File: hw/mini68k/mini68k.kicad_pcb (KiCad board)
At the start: 2 copper layers, 147.3 x 100.3 mm, 29 parts, among them J1 Jack-DC, J2 6-bit input port, J3 8-bit output port, J4 FTDI header, SW1 SW_SPDT, SW2 SW_Push, U1 HM62256BLP-7, U2 68008D, U3 L7805, U4 28C256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

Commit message: better fills
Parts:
- added J5: FTDI header COM2, Connector_PinHeader_2.54mm:PinHeader_1x06_P2.54mm_Vertical, F.Cu at (229.9, 83.8)
- added JP2: Jumper, Connector_PinHeader_2.54mm:PinHeader_1x02_P2.54mm_Vertical, F.Cu at (224.8, 71.1)
- J4: value FTDI header -> FTDI header COM1
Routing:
- net GND: track 697.5 -> 155.5 mm, vias 9 -> 12
- net VCC: track 493.9 -> 35.6 mm, vias 2 -> 3
- net TX2: track 0.00 -> 82.3 mm, vias 0 -> 1
- net RX2: track 0.00 -> 77.5 mm, vias 0 -> 1
- net A9: track 155.8 -> 131.3 mm
- net OP7: track 46.5 -> 26.5 mm
- net A4: track 146.8 -> 132.5 mm
- net A5: track 92.5 -> 81.0 mm
- net A15: track 144.1 -> 133.4 mm
- net A7: track 100.5 -> 90.1 mm
- net Net-(J5-Pad3): track 0.00 -> 10.4 mm
- net A3: track 157.4 -> 149.8 mm
- net A16: track 125.3 -> 117.8 mm
- net CLK: track 207.3 -> 199.9 mm, vias 1 -> 2
- net A6: track 89.4 -> 84.2 mm
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
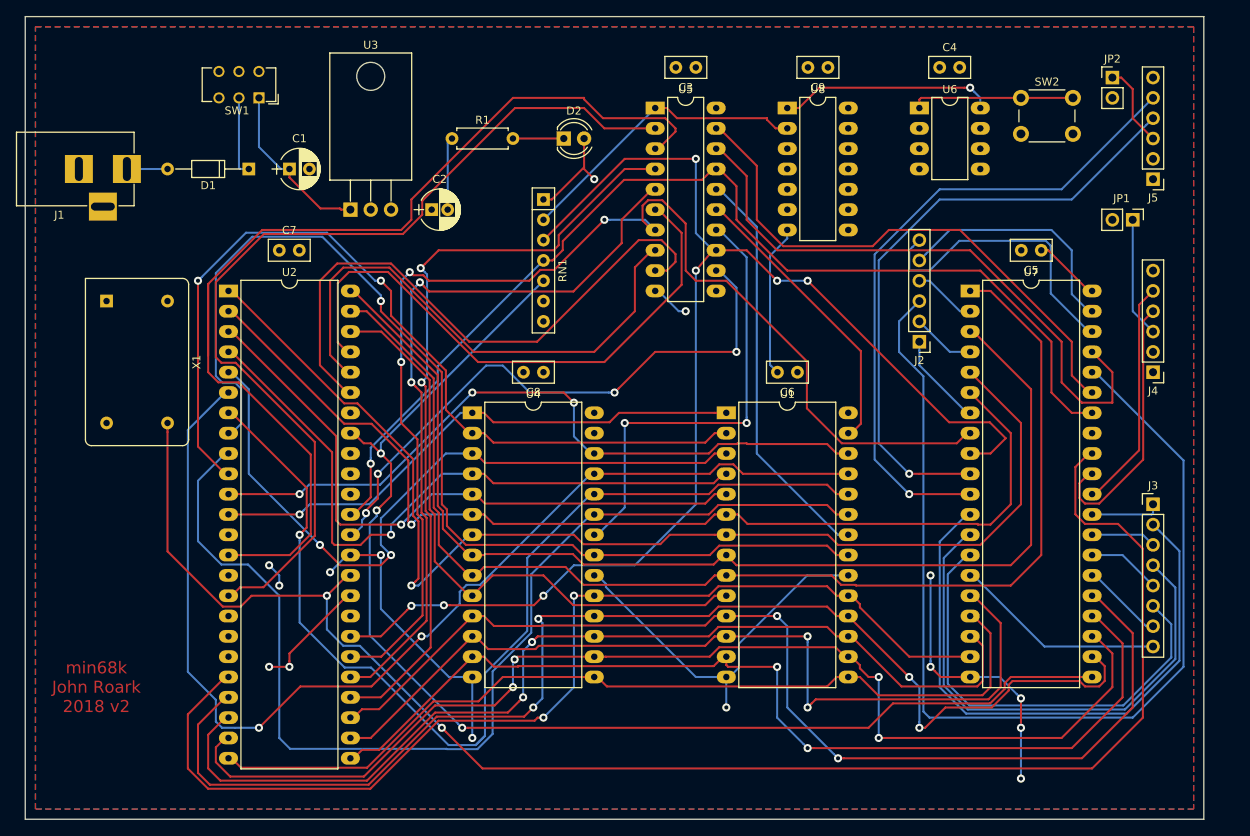
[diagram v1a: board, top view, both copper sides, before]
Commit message: more updated footprints and 3d
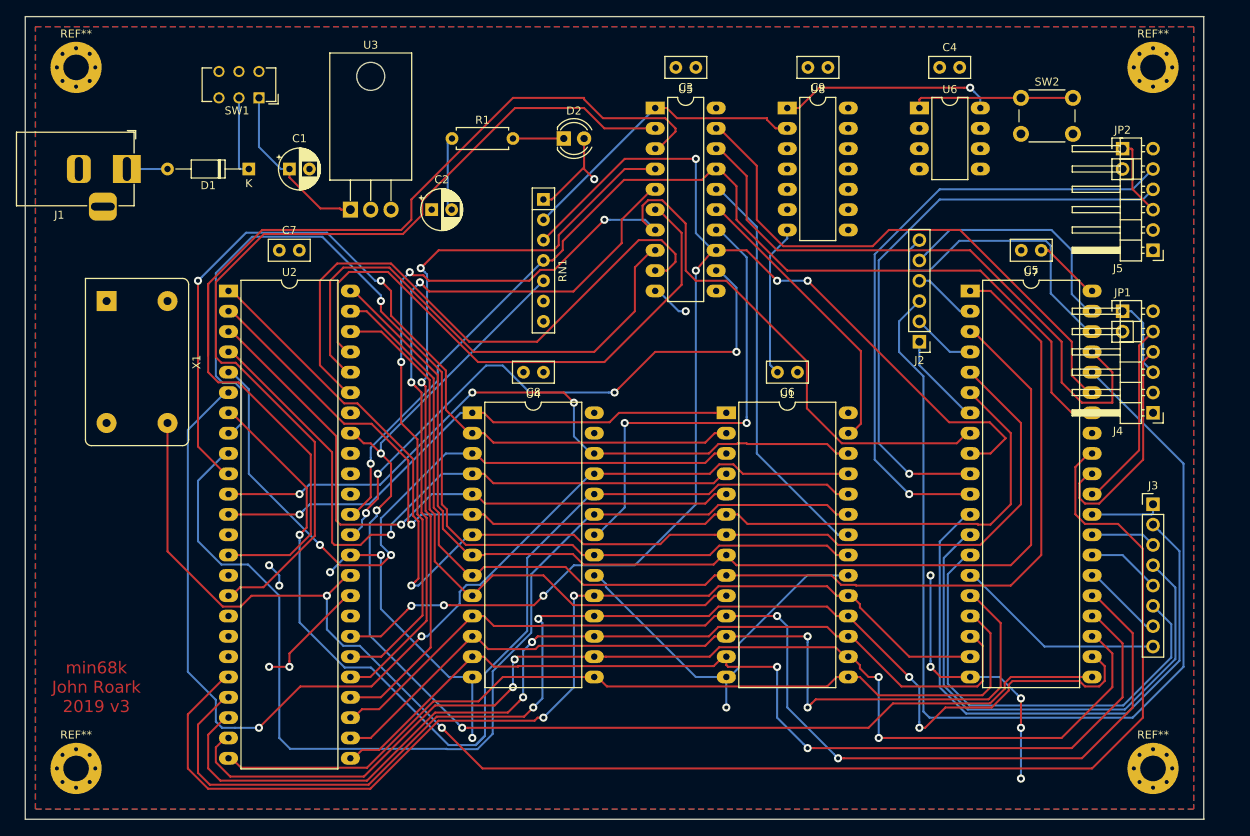
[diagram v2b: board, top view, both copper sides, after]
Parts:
- added REF**: MountingHole_3.2mm_M3_Pad_Via, MountingHole:MountingHole_3.2mm_M3_Pad_Via, F.Cu at (95.2, 157.5)
- added REF**: MountingHole_3.2mm_M3_Pad_Via, MountingHole:MountingHole_3.2mm_M3_Pad_Via, F.Cu at (95.2, 69.8)
- added REF**: MountingHole_3.2mm_M3_Pad_Via, MountingHole:MountingHole_3.2mm_M3_Pad_Via, F.Cu at (229.9, 157.5)
- added REF**: MountingHole_3.2mm_M3_Pad_Via, MountingHole:MountingHole_3.2mm_M3_Pad_Via, F.Cu at (229.9, 69.8)
- C1: footprint Capacitors_THT:CP_Radial_D5.0mm_P2.50mm -> Capacitor_THT:CP_Radial_D5.0mm_P2.50mm
- C2: footprint Capacitors_THT:CP_Radial_D5.0mm_P2.00mm -> Capacitor_THT:CP_Radial_D5.0mm_P2.50mm
- D1: footprint Diodes_THT:D_DO-35_SOD27_P10.16mm_Horizontal -> Diode_THT:D_DO-35_SOD27_P10.16mm_Horizontal
- D2: footprint LEDs:LED_D4.0mm -> LED_THT:LED_D4.0mm
- J1: footprint Connectors:BARREL_JACK -> Connector_BarrelJack:BarrelJack_Horizontal
- J4, J5: footprint Connector_PinHeader_2.54mm:PinHeader_1x06_P2.54mm_Vertical -> Connector_PinHeader_2.54mm:PinHeader_1x06_P2.54mm_Horizontal
- JP1: footprint Pin_Headers:Pin_Header_Straight_1x02_Pitch2.54mm -> Connector_PinHeader_2.54mm:PinHeader_1x02_P2.54mm_Vertical
- R1: footprint Resistors_THT:R_Axial_DIN0207_L6.3mm_D2.5mm_P7.62mm_Horizontal -> Resistor_THT:R_Axial_DIN0207_L6.3mm_D2.5mm_P7.62mm_Horizontal
- RN1: footprint Resistors_THT:R_Array_SIP7 -> Resistor_THT:R_Array_SIP7
- SW2: footprint Buttons_Switches_THT:SW_PUSH_6mm -> Button_Switch_THT:SW_PUSH_6mm
- U3: footprint TO_SOT_Packages_THT:TO-220-3_Horizontal -> Package_TO_SOT_THT:TO-220-3_Horizontal_TabDown
- X1: footprint Oscillators:Oscillator_DIP-14 -> Oscillator:Oscillator_DIP-14_LargePads
- moved JP1 11.5 mm to (226.1, 100.3), turned to 0 degrees
- moved JP2 8.98 mm to (226.1, 80.0)
- moved J5 8.89 mm to (229.9, 92.7)
- moved J4 5.08 mm to (229.9, 113.0)
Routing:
- net Net-(J4-Pad3): track 15.0 -> 9.84 mm
- net TX1: track 28.8 -> 23.7 mm
- net RX1: track 33.5 -> 28.4 mm
- net TX2: track 82.3 -> 78.6 mm
- net RX2: track 77.5 -> 73.8 mm
- net Net-(J5-Pad3): track 10.4 -> 9.84 mm
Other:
- board text added: "min68k John Roark 2019 v3"
- board text removed: "min68k John Roark 2018 v2"

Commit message: better 3d
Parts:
- J4, J5: footprint Connector_PinHeader_2.54mm:PinHeader_1x06_P2.54mm_Horizontal -> Connector_PinHeader_2.54mm:PinHeader_1x06_P2.54mm_Vertical
- SW1: footprint Buttons_Switches_THT:SW_CuK_JS202011CQN_DPDT_Straight -> Button_Switch_THT:SW_E-Switch_EG1271_DPDT

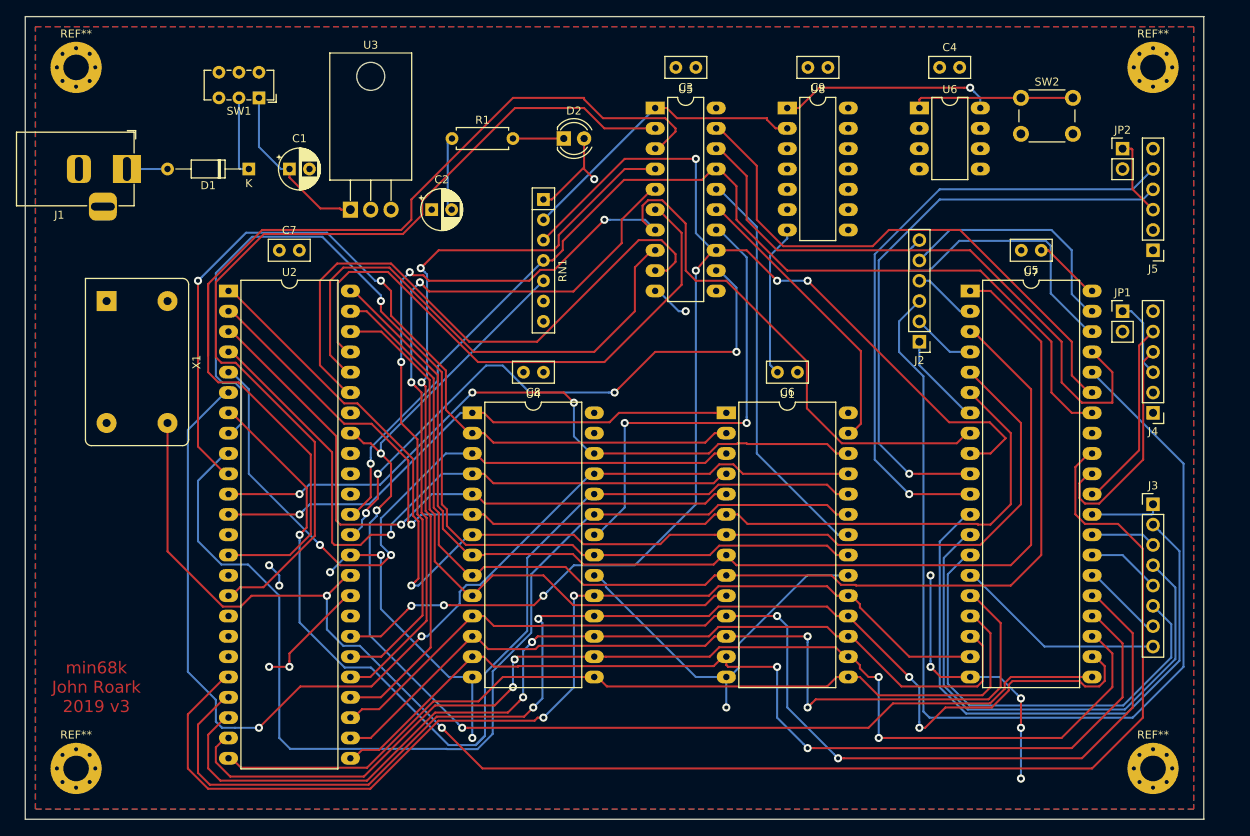
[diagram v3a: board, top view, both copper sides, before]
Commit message: jumpers for 27256/28256
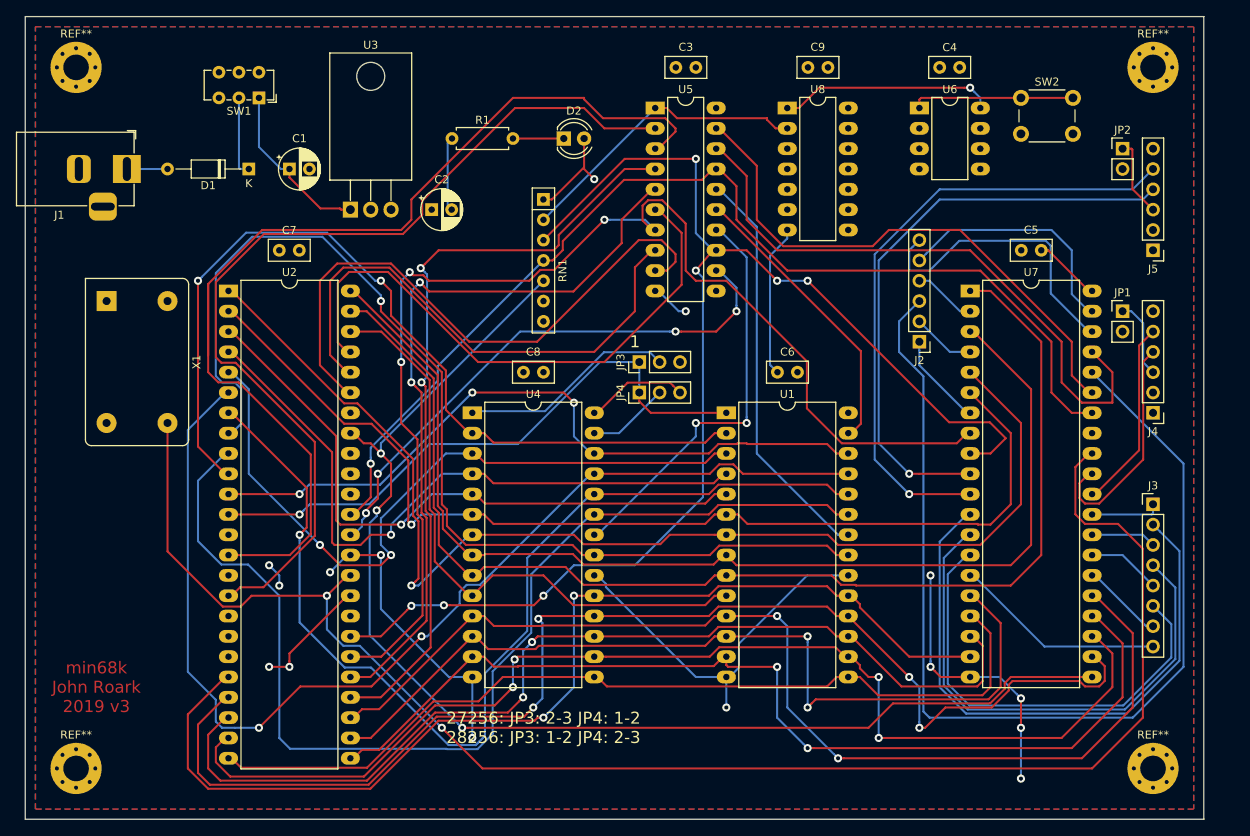
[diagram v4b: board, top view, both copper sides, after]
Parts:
- added JP3: Jumper_3_Open, Connector_PinHeader_2.54mm:PinHeader_1x03_P2.54mm_Vertical, F.Cu at (165.7, 106.7)
- added JP4: Jumper_3_Open, Connector_PinHeader_2.54mm:PinHeader_1x03_P2.54mm_Vertical, F.Cu at (165.7, 110.5)
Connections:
- U4 pad 1: A14 -> ROM_PIN1
- U4 pad 27: VCC -> ROM_PIN27
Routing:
- net ROM_PIN1: track 0.00 -> 26.7 mm
- net VCC: track 35.6 -> 48.4 mm
- net ROM_PIN27: track 0.00 -> 10.3 mm
- net A14: track 68.5 -> 75.6 mm
- net HALT: track 74.7 -> 68.9 mm
- net ROM_OE: track 57.0 -> 51.8 mm
- net DTACK: track 170.1 -> 170.8 mm
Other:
- board text added: "1"
- board text added: "27256: JP3: 2-3 JP4: 1-2 28256: JP3: 1-2 JP4: 2-3"

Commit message: labels
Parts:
- renumbered SW1 to ON, SW2 to RESET
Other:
- board text added: "GND"
- board text added: "RX"
- board text added: "TX"
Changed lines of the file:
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@@
   (general
     (thickness 1.6)
-    (drawings 7)
+    (drawings 15)
     (tracks 1110)
     (zones 0)
@@
     (descr https://www.omron.com/ecb/products/pdf/en-b3f.pdf)
     (tags "tact sw push 6mm")
-    (fp_text reference SW2 (at 3.25 -2) (layer F.SilkS)
+    (fp_text reference RESET (at 3.25 -2) (layer F.SilkS)
       (effects (font (size 1 1) (thickness 0.15)))
     )
@@
     (descr "E-Switch sub miniature slide switch, EG series, DPDT, http://spec_sheets.e-switch.com/specs/P040047.pdf")
     (tags "switch DPDT")
-    (fp_text reference SW1 (at 2.5 -1.65 180) (layer F.SilkS)
+    (fp_text reference ON (at 0 -2.54 180) (layer F.SilkS)
       (effects (font (size 1 1) (thickness 0.15)))
     )
@@
     )
   )
+  (gr_text GND (at 234.5 92.71) (layer F.SilkS)
+    (effects (font (size 1 1) (thickness 0.25)) (justify right))
+  )
+  (gr_text RX (at 232.41 85.09) (layer F.SilkS)
+    (effects (font (size 1 1) (thickness 0.25)))
+  )
+  (gr_text TX (at 232.41 82.55) (layer F.SilkS)
+    (effects (font (size 1 1) (thickness 0.25)))
+  )
+  (gr_text GND (at 234.5 113.03) (layer F.SilkS)
+    (effects (font (size 1 1) (thickness 0.25)) (justify right))
+  )
+  (gr_text RX (at 232.41 105.41) (layer F.SilkS)
+    (effects (font (size 1 1) (thickness 0.25)))
+  )
+  (gr_text TX (at 232.41 102.87) (layer F.SilkS)
+    (effects (font (size 1 1) (thickness 0.25)))
+  )
+  (gr_text 1 (at 232.41 124.46) (layer F.SilkS)
+    (effects (font (size 1.5 1.5) (thickness 0.3)))
+  )
+  (gr_text 1 (at 198.12 104.14) (layer F.SilkS)
+    (effects (font (size 1.5 1.5) (thickness 0.3)))
+  )
   (gr_text "27256: JP3: 2-3 JP4: 1-2\n28256: JP3: 1-2 JP4: 2-3" (at 153.67 152.4) (layer F.SilkS)

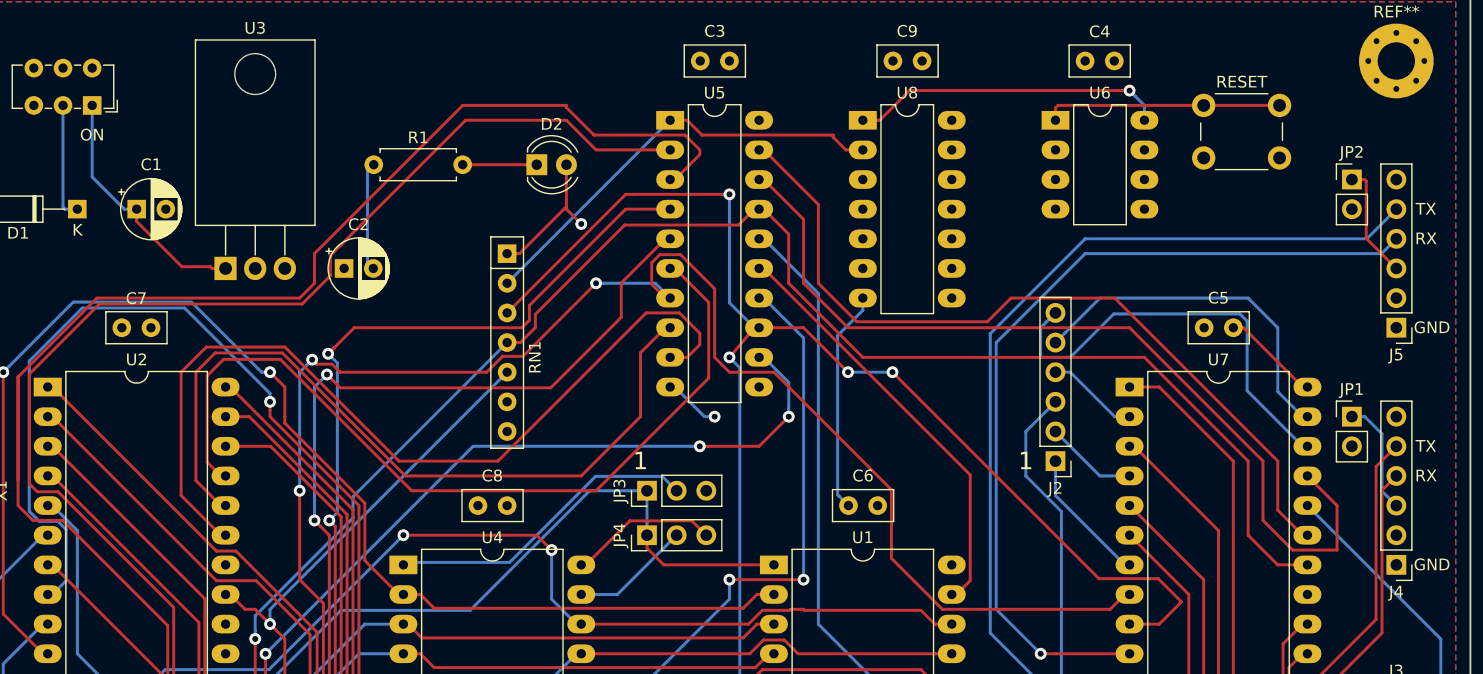
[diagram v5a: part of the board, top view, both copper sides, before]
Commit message: correct ram pinout... update symbols
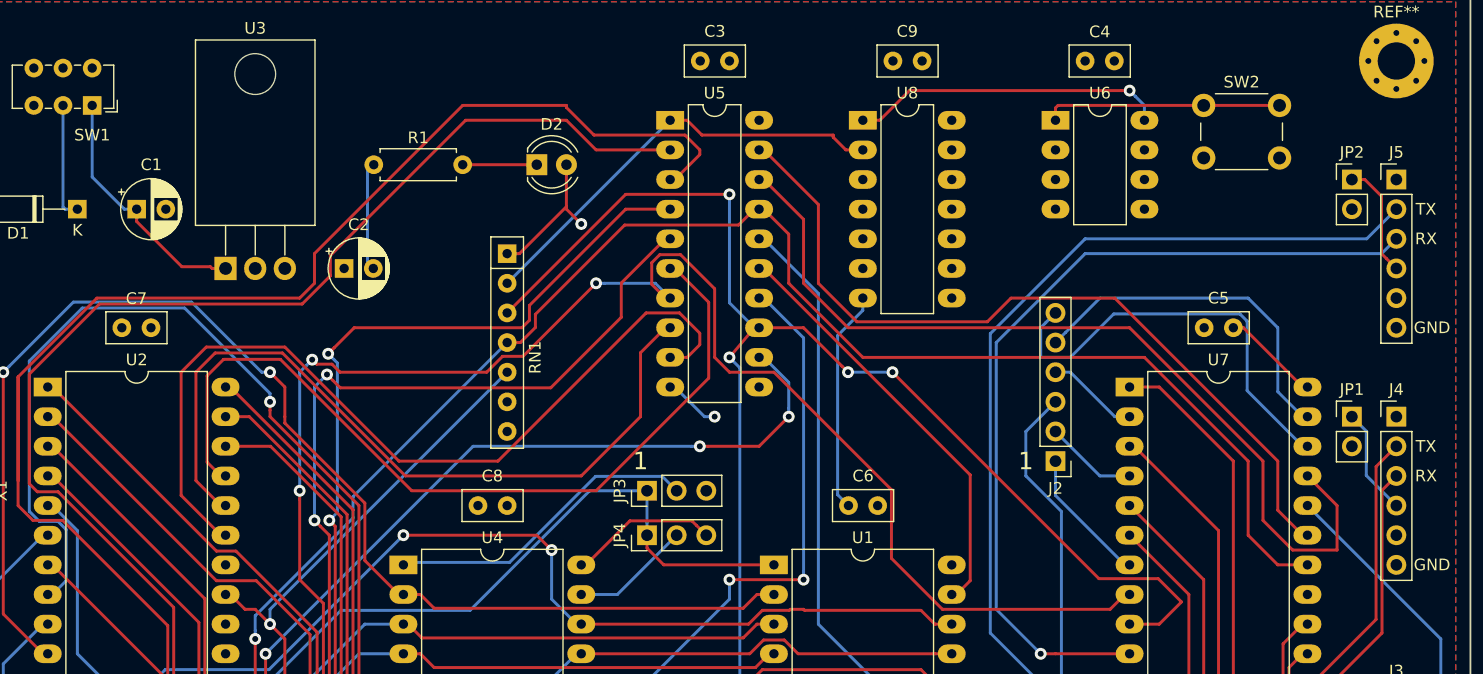
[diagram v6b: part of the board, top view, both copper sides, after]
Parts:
- U4: value 28C256 -> 28C256/27C256
- moved J4 12.7 mm to (229.9, 100.3), turned to 0 degrees
- moved J5 12.7 mm to (229.9, 80.0), turned to 0 degrees
- renumbered ON to SW1, RESET to SW2
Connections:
- J4 pad 1: GND -> Net-(J4-Pad1)
- J4 pad 2: Net-(J4-Pad2) -> TX1
- J4 pad 3: Net-(J4-Pad3) -> RX1
- J4 pad 4: RX1 -> Net-(J4-Pad4)
- J4 pad 5: TX1 -> Net-(J4-Pad5)
- J4 pad 6: Net-(J4-Pad6) -> GND
- J5 pad 1: GND -> Net-(J5-Pad1)
- J5 pad 2: Net-(J5-Pad2) -> TX2
- J5 pad 3: Net-(J5-Pad3) -> RX2
- J5 pad 4: RX2 -> Net-(J5-Pad4)
- J5 pad 5: TX2 -> Net-(J5-Pad5)
- J5 pad 6: Net-(J5-Pad6) -> GND
- JP1 pad 1: Net-(J4-Pad3) -> Net-(J4-Pad4)
- JP2 pad 1: Net-(J5-Pad3) -> Net-(J5-Pad4)
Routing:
- net Net-(J4-Pad3): track 9.84 -> 0.00 mm
- net Net-(J5-Pad4): track 0.00 -> 9.84 mm
- net Net-(J5-Pad3): track 9.84 -> 0.00 mm
- net Net-(J4-Pad4): track 0.00 -> 9.23 mm
